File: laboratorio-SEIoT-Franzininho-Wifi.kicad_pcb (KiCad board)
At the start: 2 copper layers, 179.8 x 142.6 mm, 141 parts, among them J1 Conn_01x20, J2 Conn_01x20, J3 Grove, J4 Grove, M1 Motor_Servo, Q1 BC547, SW1 SW_Push_Dual, SW10 SW_Push_Dual, SW11 SW_Push_Dual, SW12 SW_Push_Dual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

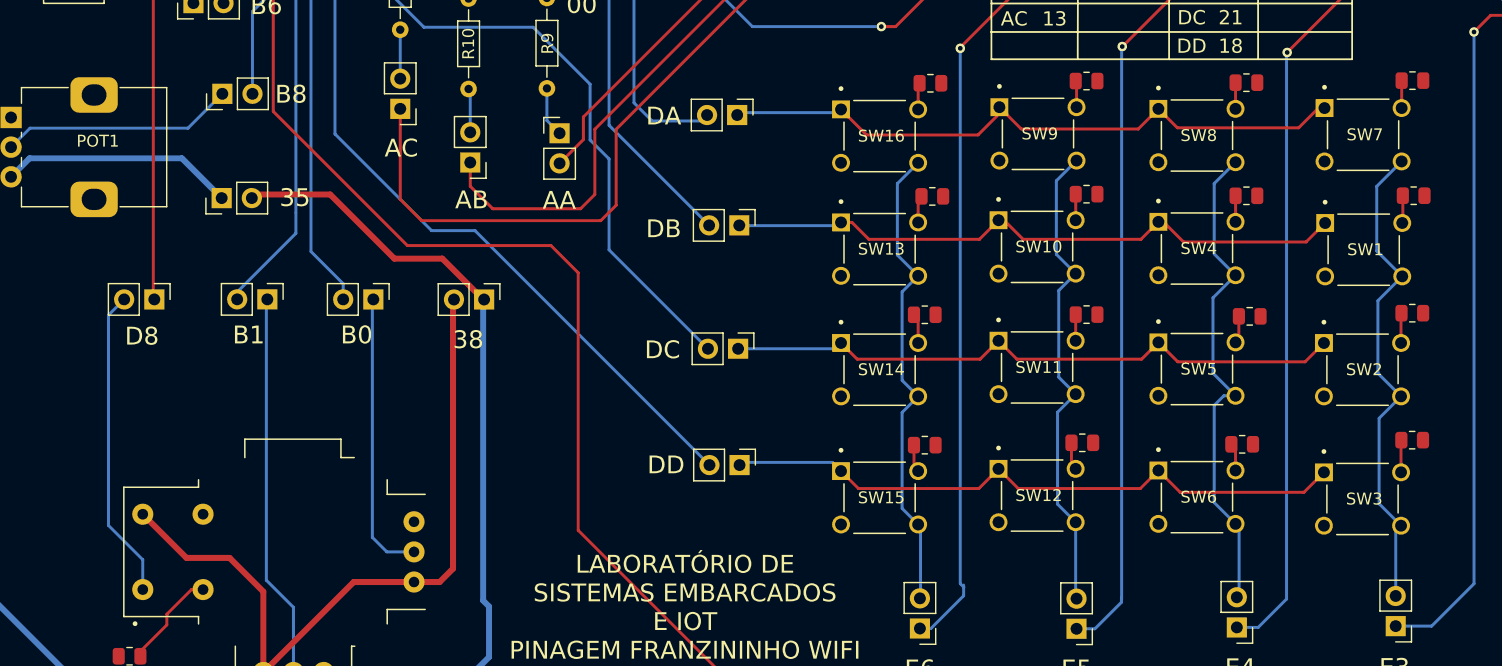
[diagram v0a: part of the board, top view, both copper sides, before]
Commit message: correção de conexão no display de 7 segmentos
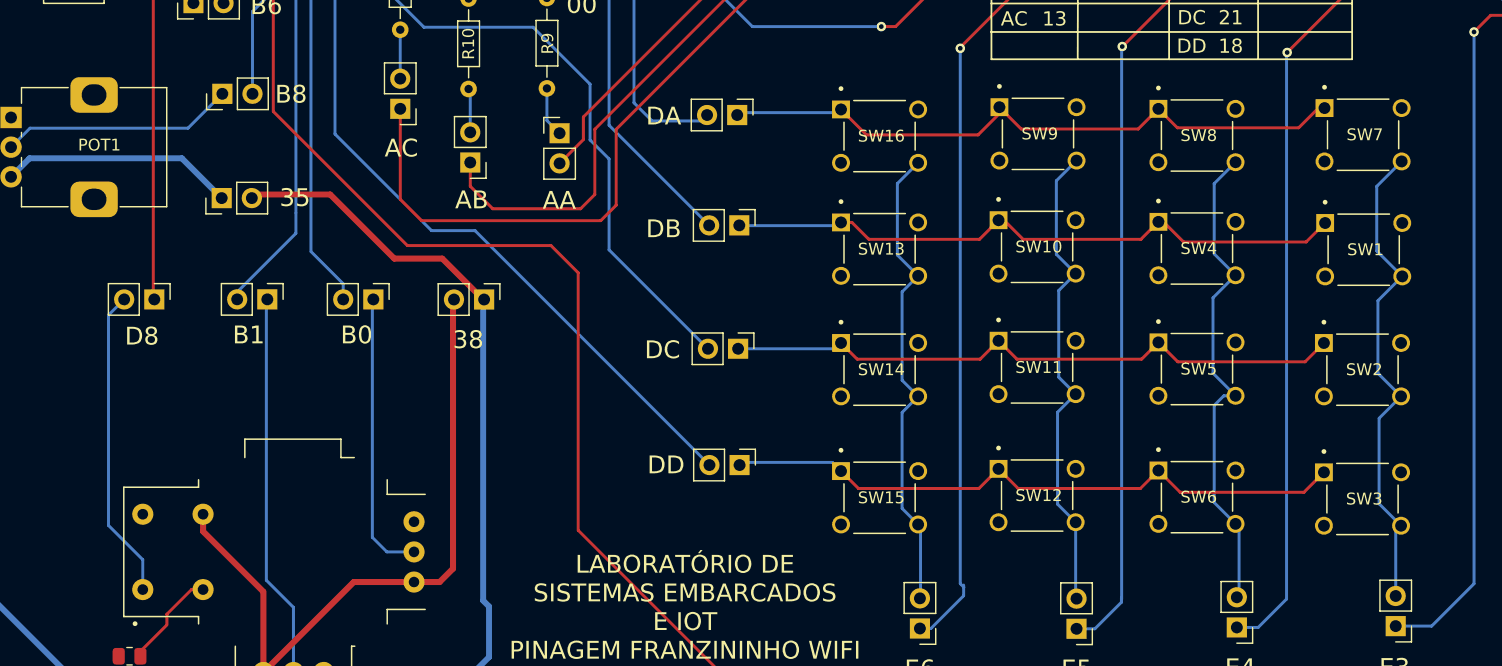
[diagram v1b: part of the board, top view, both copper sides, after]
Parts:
- removed R13, R14, R15, R16, R17, R18, R19, R20, R21, R22, R23, R24, R25, R26, R27, R28: R, Resistor_SMD:R_0805_2012Metric
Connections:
- SW1 pad 2: Net-(R14-Pad1) -> unconnected-(SW1-Pad2)
- SW10 pad 2: Net-(R22-Pad1) -> unconnected-(SW10-Pad2)
- SW11 pad 2: Net-(R23-Pad1) -> unconnected-(SW11-Pad2)
- SW12 pad 2: Net-(R24-Pad1) -> unconnected-(SW12-Pad2)
- SW13 pad 2: Net-(R25-Pad1) -> unconnected-(SW13-Pad2)
- SW14 pad 2: Net-(R26-Pad1) -> unconnected-(SW14-Pad2)
- SW15 pad 2: Net-(R27-Pad1) -> unconnected-(SW15-Pad2)
- SW16 pad 2: Net-(R28-Pad1) -> unconnected-(SW16-Pad2)
- SW2 pad 2: Net-(R15-Pad1) -> unconnected-(SW2-Pad2)
- SW3 pad 2: Net-(R16-Pad1) -> unconnected-(SW3-Pad2)
- SW4 pad 2: Net-(R17-Pad1) -> unconnected-(SW4-Pad2)
- SW5 pad 2: Net-(R18-Pad1) -> unconnected-(SW5-Pad2)
- SW6 pad 2: Net-(R19-Pad1) -> unconnected-(SW6-Pad2)
- SW7 pad 2: Net-(R13-Pad1) -> unconnected-(SW7-Pad2)
- SW8 pad 2: Net-(R20-Pad1) -> unconnected-(SW8-Pad2)
- SW9 pad 2: Net-(R21-Pad1) -> unconnected-(SW9-Pad2)
- U2 pad 3: GND -> unconnected-(U2-CC-Pad3)
- U4 pad B1B: Net-(Enable38-Pin_2) -> (no net)
- U4 pad B2B: (no net) -> Net-(Enable38-Pin_2)
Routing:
- net Net-(Enable38-Pin_2): track 61.9 -> 57.7 mm
- net Net-(R16-Pad1): track 2.69 -> 0.00 mm
- net Net-(R15-Pad1): track 2.48 -> 0.00 mm
- net Net-(R13-Pad1): track 2.31 -> 0.00 mm
- net Net-(R14-Pad1): track 2.25 -> 0.00 mm
- net Net-(R23-Pad1): track 2.20 -> 0.00 mm
- net Net-(R20-Pad1): track 2.20 -> 0.00 mm
- net Net-(R22-Pad1): track 2.19 -> 0.00 mm
- net Net-(R17-Pad1): track 2.19 -> 0.00 mm
- net Net-(R21-Pad1): track 2.13 -> 0.00 mm
- net Net-(R28-Pad1): track 2.08 -> 0.00 mm
- net Net-(R26-Pad1): track 2.03 -> 0.00 mm
- net Net-(R25-Pad1): track 1.91 -> 0.00 mm
- net Net-(R18-Pad1): track 1.91 -> 0.00 mm
- net Net-(R19-Pad1): track 1.85 -> 0.00 mm
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
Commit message: adição da licensa
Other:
- board text added: "Licensed under CERN-OHL-S v2"
- board text added: "SOURCE: github.com/Franzininho/laboratorio-SEIoT-Franzininho-Wifi"
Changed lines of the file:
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@@
   (gr_rect (start 25.7408 20.3454) (end 205.5008 162.9018)
     (stroke (width 0.15) (type solid)) (fill none) (layer "Edge.Cuts"))
+  (gr_text "SOURCE: github.com/Franzininho/laboratorio-SEIoT-Franzininho-Wifi" (at 151.1554 161.3154) (layer "B.SilkS")
+    (effects (font (size 1 1) (thickness 0.15)) (justify left bottom mirror))
+  )
   (gr_text "C0" (at 136.25 86.9) (layer "F.SilkS")
     (effects (font (size 1.2 1.2) (thickness 0.25)))
@@
     (effects (font (size 0.8 0.8) (thickness 0.2) bold))
   )
+  (gr_text "Licensed under CERN-OHL-S v2" (at 110.0836 161.5186) (layer "F.SilkS")
+    (effects (font (size 1 1) (thickness 0.15)) (justify left bottom))
+  )
   (gr_text "E5" (at 118.5 155.6) (layer "F.SilkS")

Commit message: certificação adicionada
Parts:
- added G1: LOGO, LOGO, F.Cu at (85.4, 157.4)
